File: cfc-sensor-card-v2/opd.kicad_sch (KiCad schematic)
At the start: 73 parts, among them Q1 DMP2240UDM, Q2 PMV45EN, Q3 DMP3050LVT-7, Q4 DMP3050LVT-7, Q5 PMV45EN, U2 MAX7310, U3 MIC842LYC5, U4 MIC842LYC5, U5 MAX4211FETE

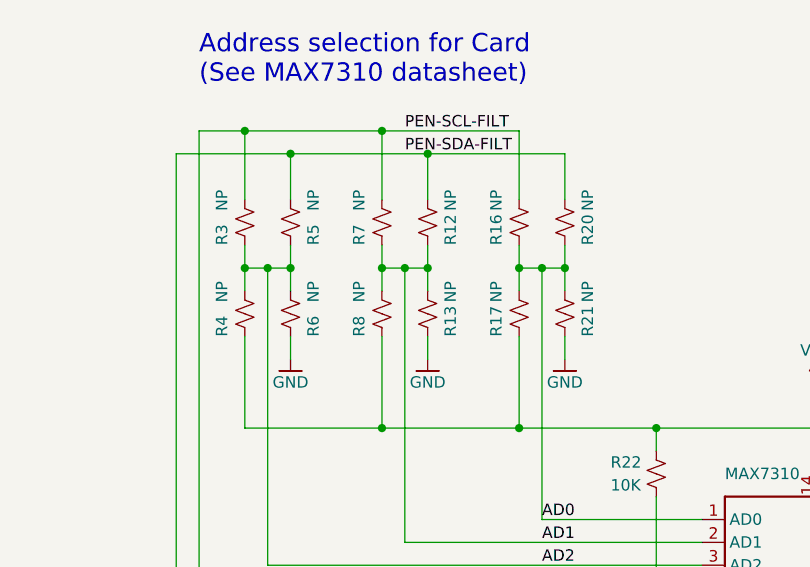
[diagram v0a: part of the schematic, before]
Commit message: added OPD address resistors
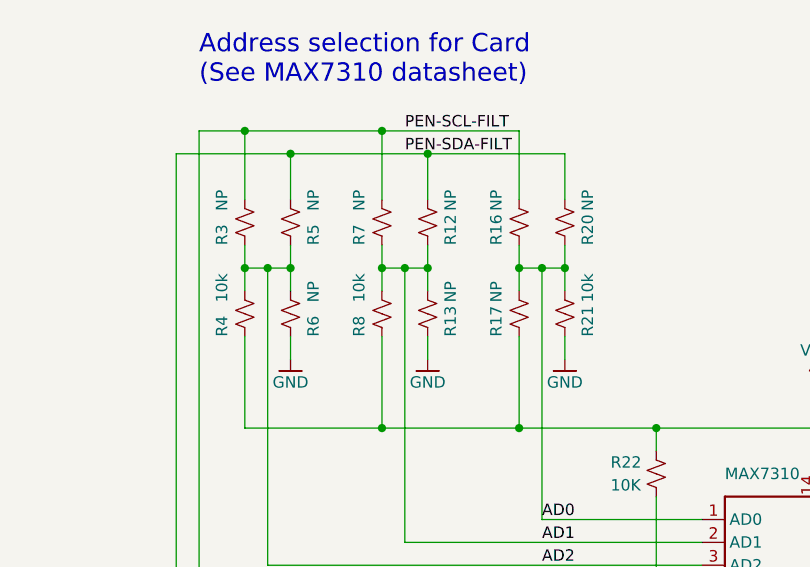
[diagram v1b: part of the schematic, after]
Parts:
- R21, R4, R8: value NP -> 10k
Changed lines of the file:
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@@
       (effects (font (size 1.27 1.27)) (justify left))
     )
-    (property "Value" "NP" (id 1) (at 43.18 85.09 90)
+    (property "Value" "10k" (id 1) (at 43.18 85.09 90)
       (effects (font (size 1.27 1.27)) (justify left))
     )
@@
       (effects (font (size 1.27 1.27)) (justify left))
     )
-    (property "Value" "NP" (id 1) (at 83.82 85.09 90)
+    (property "Value" "10k" (id 1) (at 83.82 85.09 90)
       (effects (font (size 1.27 1.27)) (justify left))
     )
@@
       (effects (font (size 1.27 1.27)) (justify left))
     )
-    (property "Value" "NP" (id 1) (at 58.42 85.09 90)
-      (effects (font (size 1.27 1.27)) (justify left))
-    )
+    (property "Value" "10k" (id 1) (at 58.42 85.09 90)
+      (effects (font (size 1.27 1.27)) (justify left))
+    )

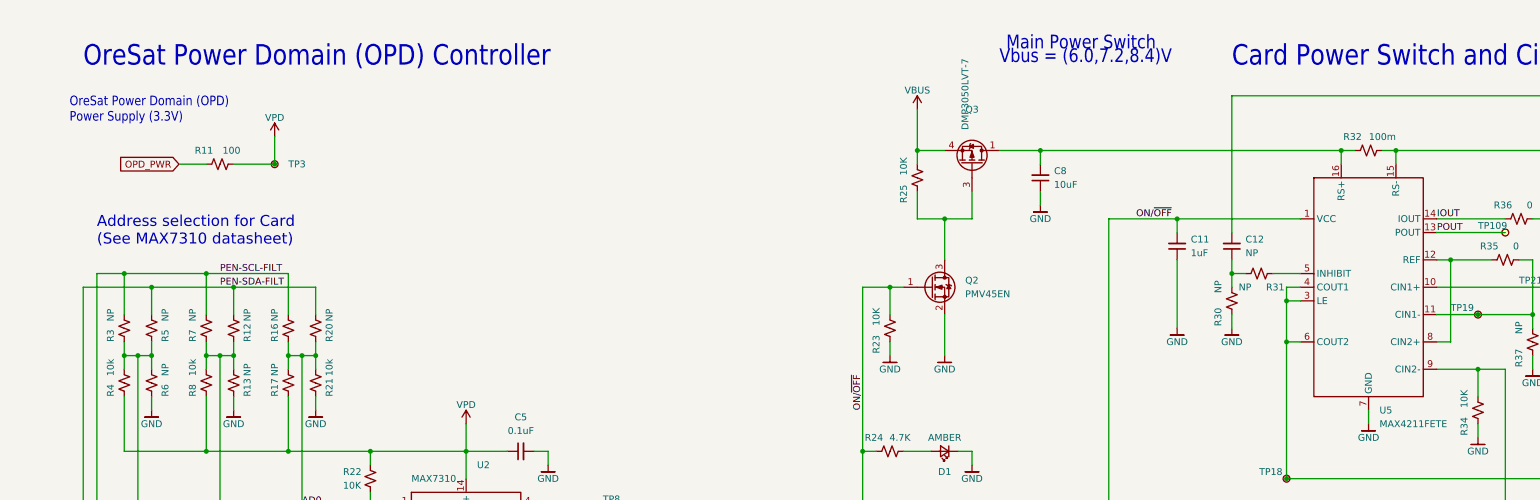
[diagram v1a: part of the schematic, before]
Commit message: OPD CB shunt resistor is 10m, not 100m. Cleanup documentation. Also clean up documentation on other pages.
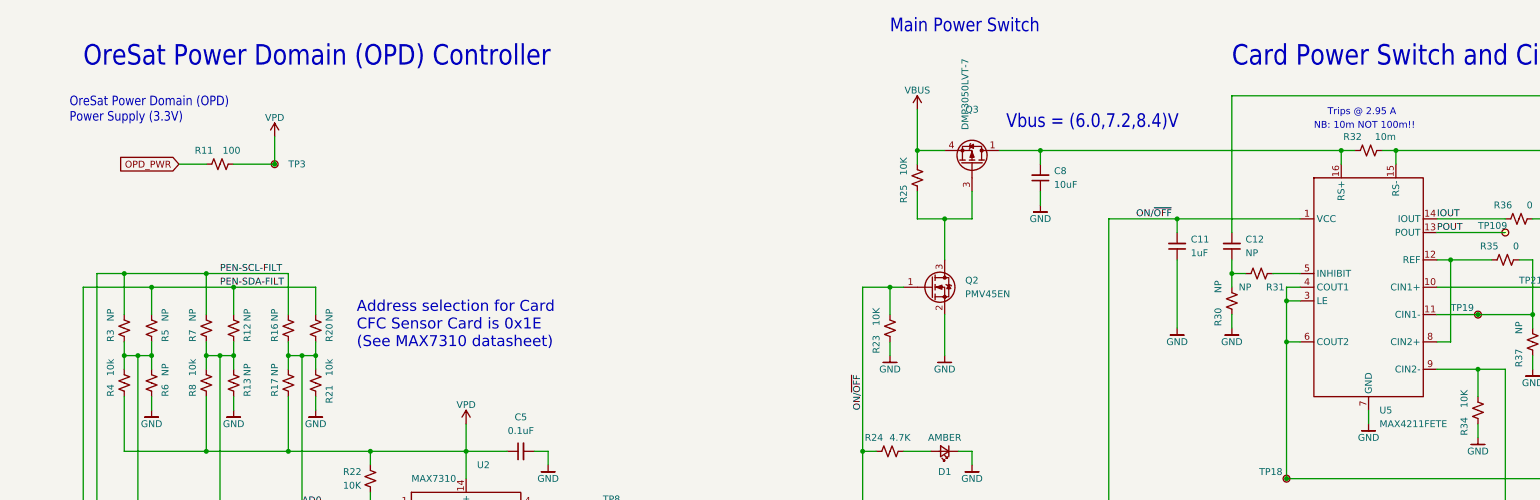
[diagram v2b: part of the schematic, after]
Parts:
- R32: value 100m -> 10m
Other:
- note added: "Address selection for Card CFC Sensor Card is 0x1E (See MAX7310 datasheet)"
- note added: "NB: 10m NOT 100m!!"
- note added: "Trips @ 2.95 A"
- note removed: "Address selection for Card (See MAX7310 datasheet)"
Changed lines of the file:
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@@
     (stroke (width 0) (type default) (color 0 0 0 0))
   )
-  (text "Vbus = (6.0,7.2,8.4)V" (at 208.28 27.305 180)
+  (text "Trips @ 2.95 A" (at 269.24 36.83 0)
+    (effects (font (size 1.27 1.27)) (justify left bottom))
+  )
+  (text "Vbus = (6.0,7.2,8.4)V" (at 209.55 39.37 180)
     (effects (font (size 2.54 2.159)) (justify left bottom))
   )
   (text "OreSat Power Domain (OPD)\nPower Supply (3.3V)" (at 35.56 38.1 180)
     (effects (font (size 1.778 1.5113)) (justify left bottom))
+  )
+  (text "NB: 10m NOT 100m!!" (at 266.7 39.37 0)
+    (effects (font (size 1.27 1.27)) (justify left bottom))
   )
   (text "OreSat Power Domain (OPD) Controller" (at 38.1 27.94 180)
@@
     (effects (font (size 1.778 1.5113)) (justify left bottom))
   )
-  (text "Address selection for Card\n(See MAX7310 datasheet)"
-    (at 40.64 60.96 0)
+  (text "Address selection for Card\nCFC Sensor Card is 0x1E\n(See MAX7310 datasheet)"
+    (at 88.9 80.01 0)
     (effects (font (size 2.032 2.032)) (justify left bottom))
   )
@@
     (effects (font (size 2.54 2.159)) (justify right bottom))
   )
-  (text "Main Power Switch" (at 209.55 24.765 180)
+  (text "Main Power Switch" (at 187.96 21.59 180)
     (effects (font (size 2.54 2.159)) (justify left bottom))
   )
@@
       (effects (font (size 1.27 1.27)) (justify left))
     )
-    (property "Value" "100m" (id 1) (at 281.94 40.64 90)
+    (property "Value" "10m" (id 1) (at 281.94 40.64 90)
       (effects (font (size 1.27 1.27)) (justify left))
     )
@@
   (symbol (lib_id "Device:R_Small_US") (at 81.28 86.36 0) (unit 1)
     (in_bom yes) (on_board yes)
-    (property "Reference" "R21" (id 0) (at 83.82 88.9 90)
-      (effects (font (size 1.27 1.27)) (justify left))
-    )
+    (property "Reference" "R21" (id 0) (at 83.82 90.17 90)
+      (effects (font (size 1.27 1.27)) (justify left))
+    )

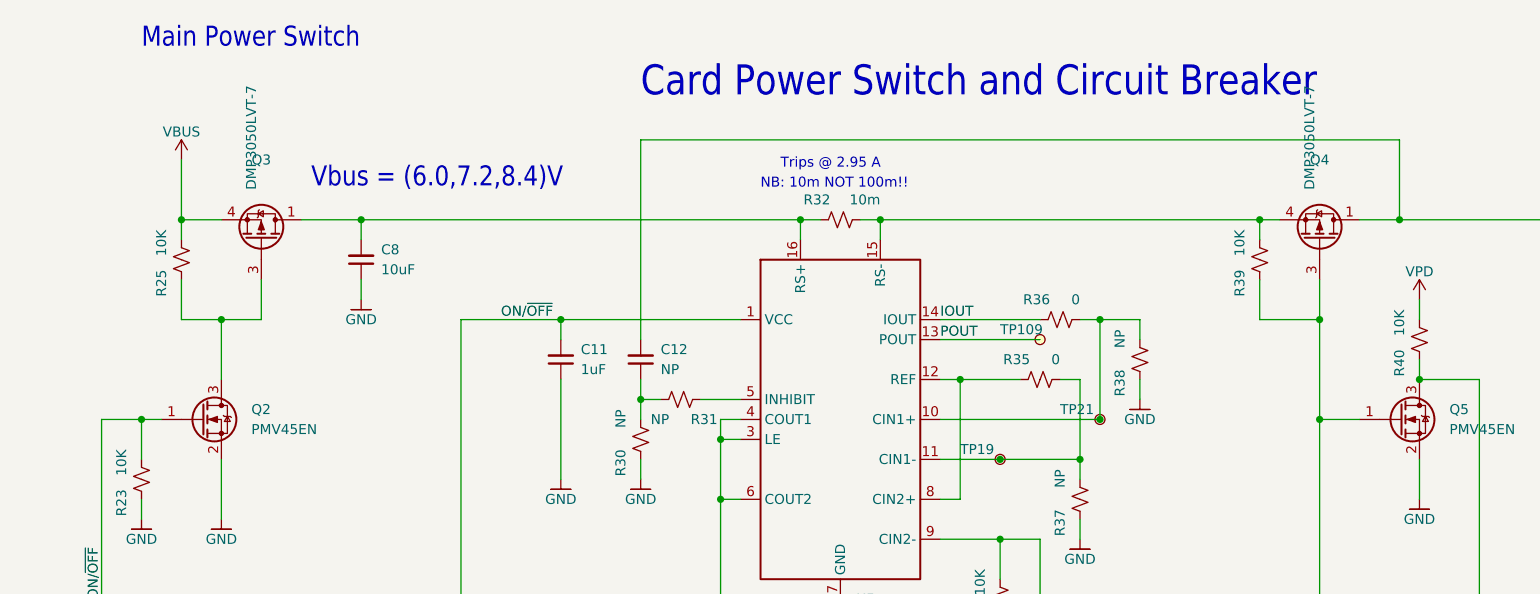
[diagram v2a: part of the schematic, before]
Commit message: Fixed wrong NPs in CFC sensor card OPD. Updated to KiCAD 7.
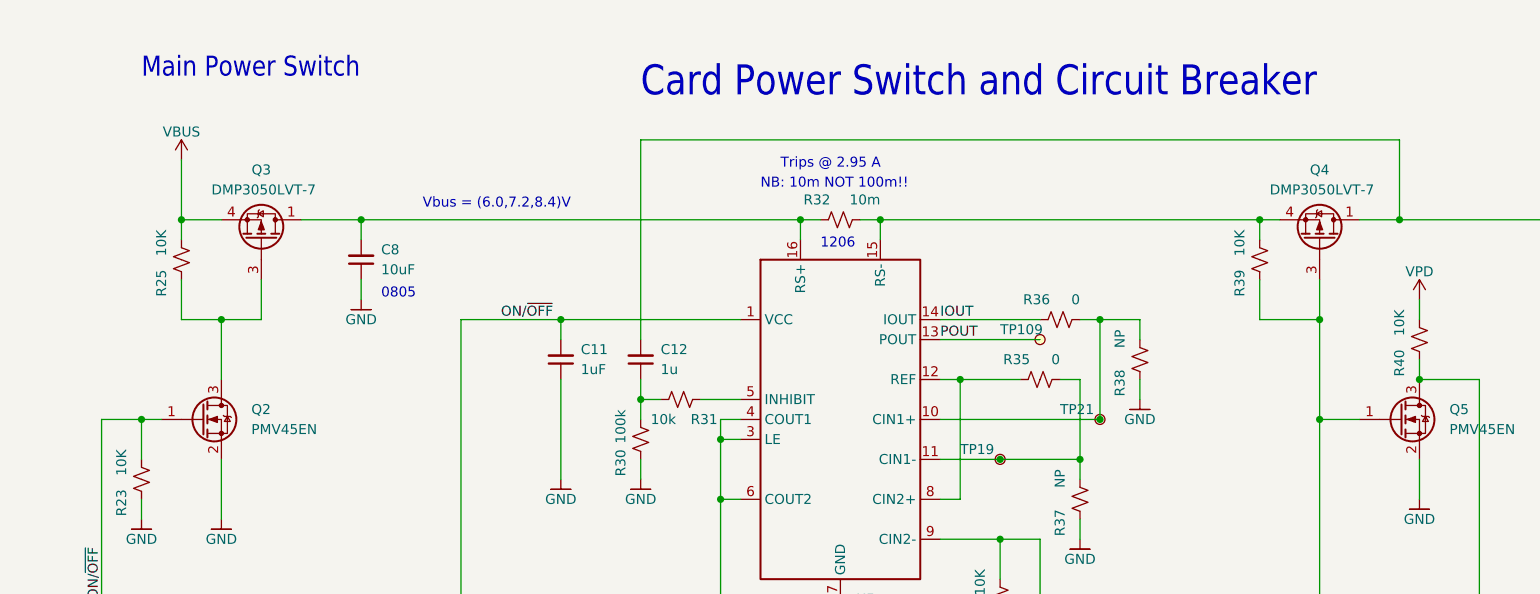
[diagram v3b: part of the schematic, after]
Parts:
- C12: value NP -> 1u
- R30: value NP -> 100k
- R31: value NP -> 10k
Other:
- note added: "0805"
- note added: "1206"

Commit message: Added soft start to sensor card and cleaned up some KiCad warnings
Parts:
- TP10, TP109, TP11, TP12, TP13, TP14, TP15, TP18, TP19, TP21, TP22, TP3, TP4, TP5, TP6, TP7, TP8, TP9: footprint oresat-misc:TestPoint-MinTH -> oresat-misc:TestPoint-0.75mm-th
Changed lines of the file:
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@@
       (effects (font (size 1.27 1.27)) hide)
     )
-    (property "Footprint" "oresat-misc:TestPoint-MinTH" (at 139.7 121.92 0)
+    (property "Footprint" "oresat-misc:TestPoint-0.75mm-th" (at 139.7 121.92 0)
       (effects (font (size 1.27 1.27)) hide)
     )
@@
       (effects (font (size 1.27 1.27)) hide)
     )
-    (property "Footprint" "oresat-misc:TestPoint-MinTH" (at 109.22 238.76 0)
+    (property "Footprint" "oresat-misc:TestPoint-0.75mm-th" (at 109.22 238.76 0)
       (effects (font (size 1.27 1.27)) hide)
     )
@@
       (effects (font (size 1.27 1.27)) hide)
     )
-    (property "Footprint" "oresat-misc:TestPoint-MinTH" (at 139.7 116.84 0)
+    (property "Footprint" "oresat-misc:TestPoint-0.75mm-th" (at 139.7 116.84 0)
       (effects (font (size 1.27 1.27)) hide)
     )
@@
       (effects (font (size 1.27 1.27)) hide)
     )
-    (property "Footprint" "oresat-misc:TestPoint-MinTH" (at 139.7 119.38 0)
+    (property "Footprint" "oresat-misc:TestPoint-0.75mm-th" (at 139.7 119.38 0)
       (effects (font (size 1.27 1.27)) hide)
     )
@@
       (effects (font (size 1.27 1.27)) hide)
     )
-    (property "Footprint" "oresat-misc:TestPoint-MinTH" (at 302.26 53.34 0)
+    (property "Footprint" "oresat-misc:TestPoint-0.75mm-th" (at 302.26 53.34 0)
       (effects (font (size 1.27 1.27)) hide)
     )
@@
       (effects (font (size 1.27 1.27)) hide)
     )
-    (property "Footprint" "oresat-misc:TestPoint-MinTH" (at 73.66 40.64 0)
+    (property "Footprint" "oresat-misc:TestPoint-0.75mm-th" (at 73.66 40.64 0)
       (effects (font (size 1.27 1.27)) hide)
     )
@@
       (effects (font (size 1.27 1.27)) hide)
     )
-    (property "Footprint" "oresat-misc:TestPoint-MinTH" (at 261.62 99.06 0)
+    (property "Footprint" "oresat-misc:TestPoint-0.75mm-th" (at 261.62 99.06 0)
       (effects (font (size 1.27 1.27)) hide)
     )
@@
       (effects (font (size 1.27 1.27)) hide)
     )
-    (property "Footprint" "oresat-misc:TestPoint-MinTH" (at 139.7 111.76 0)
+    (property "Footprint" "oresat-misc:TestPoint-0.75mm-th" (at 139.7 111.76 0)
       (effects (font (size 1.27 1.27)) hide)
     )
@@
       (effects (font (size 1.27 1.27)) hide)
     )
-    (property "Footprint" "oresat-misc:TestPoint-MinTH" (at 109.22 190.5 0)
+    (property "Footprint" "oresat-misc:TestPoint-0.75mm-th" (at 109.22 190.5 0)
       (effects (font (size 1.27 1.27)) hide)
     )
@@
       (effects (font (size 1.27 1.27)) hide)
     )
-    (property "Footprint" "oresat-misc:TestPoint-MinTH" (at 139.7 106.68 0)
+    (property "Footprint" "oresat-misc:TestPoint-0.75mm-th" (at 139.7 106.68 0)
       (effects (font (size 1.27 1.27)) hide)
     )
@@
       (effects (font (size 1.27 1.27)) hide)
     )
-    (property "Footprint" "oresat-misc:TestPoint-MinTH" (at 83.82 114.3 0)
+    (property "Footprint" "oresat-misc:TestPoint-0.75mm-th" (at 83.82 114.3 0)
       (effects (font (size 1.27 1.27)) hide)
     )
@@
       (effects (font (size 1.27 1.27)) hide)
     )
-    (property "Footprint" "oresat-misc:TestPoint-MinTH" (at 309.88 63.5 0)
+    (property "Footprint" "oresat-misc:TestPoint-0.75mm-th" (at 309.88 63.5 0)
       (effects (font (size 1.27 1.27)) hide)
     )
@@
       (effects (font (size 1.27 1.27)) hide)
     )
-    (property "Footprint" "oresat-misc:TestPoint-MinTH" (at 375.92 38.1 0)
+    (property "Footprint" "oresat-misc:TestPoint-0.75mm-th" (at 375.92 38.1 0)
       (effects (font (size 1.27 1.27)) hide)
     )
@@
       (effects (font (size 1.27 1.27)) hide)
     )
-    (property "Footprint" "oresat-misc:TestPoint-MinTH" (at 83.82 116.84 0)
+    (property "Footprint" "oresat-misc:TestPoint-0.75mm-th" (at 83.82 116.84 0)
       (effects (font (size 1.27 1.27)) hide)
     )
@@
       (effects (font (size 1.27 1.27)) hide)
     )
-    (property "Footprint" "oresat-misc:TestPoint-MinTH" (at 139.7 104.14 0)
+    (property "Footprint" "oresat-misc:TestPoint-0.75mm-th" (at 139.7 104.14 0)
       (effects (font (size 1.27 1.27)) hide)
     )
@@
       (effects (font (size 1.27 1.27)) hide)
     )
-    (property "Footprint" "oresat-misc:TestPoint-MinTH" (at 297.18 68.58 0)
+    (property "Footprint" "oresat-misc:TestPoint-0.75mm-th" (at 297.18 68.58 0)
       (effects (font (size 1.27 1.27)) hide)
     )
@@
       (effects (font (size 1.27 1.27)) hide)
     )
-    (property "Footprint" "oresat-misc:TestPoint-MinTH" (at 139.7 114.3 0)
+    (property "Footprint" "oresat-misc:TestPoint-0.75mm-th" (at 139.7 114.3 0)
       (effects (font (size 1.27 1.27)) hide)
     )
@@
       (effects (font (size 1.27 1.27)) hide)
     )
-    (property "Footprint" "oresat-misc:TestPoint-MinTH" (at 139.7 109.22 0)
-      (effects (font (size 1.27 1.27)) hide)
-    )
+    (property "Footprint" "oresat-misc:TestPoint-0.75mm-th" (at 139.7 109.22 0)
+      (effects (font (size 1.27 1.27)) hide)
+    )
